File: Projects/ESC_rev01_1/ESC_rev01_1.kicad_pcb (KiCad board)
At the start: 2 copper layers, 65 x 56 mm, 4 parts

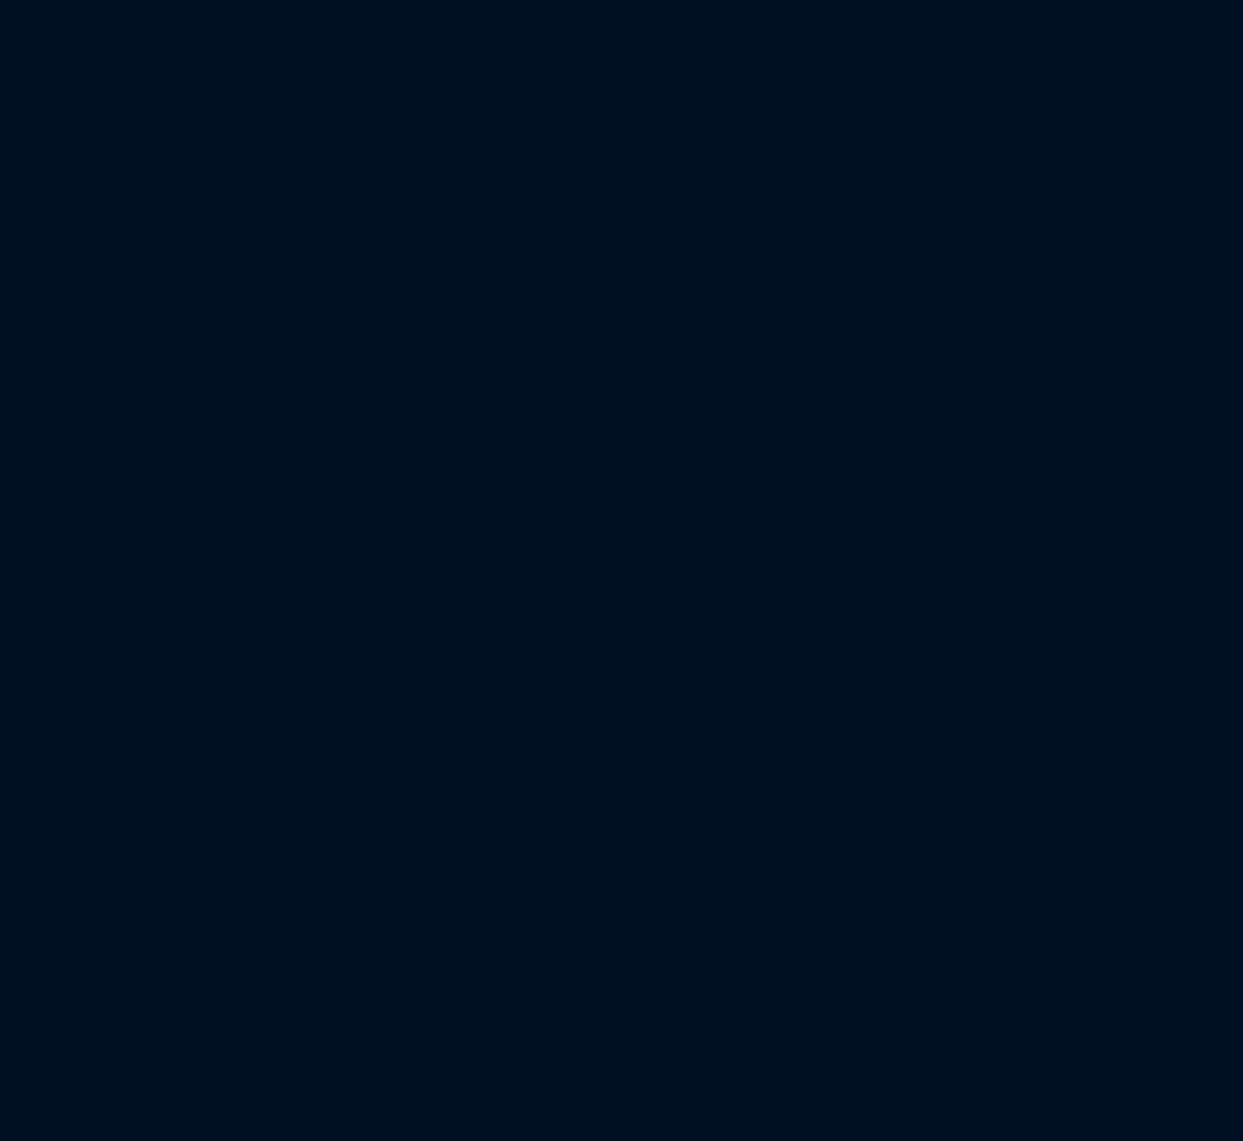
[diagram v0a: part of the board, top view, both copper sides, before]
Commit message: Update 07
Schematic is ready
INPUT PROTECTION schematic created
MOSFETs schematic created
CAN schematic created
FILTERs schematic created
MECHANICAL schematic created
STEP-DOWN schematic created
Footprints, 3D models are added and corrected (major issues)
Component placement started
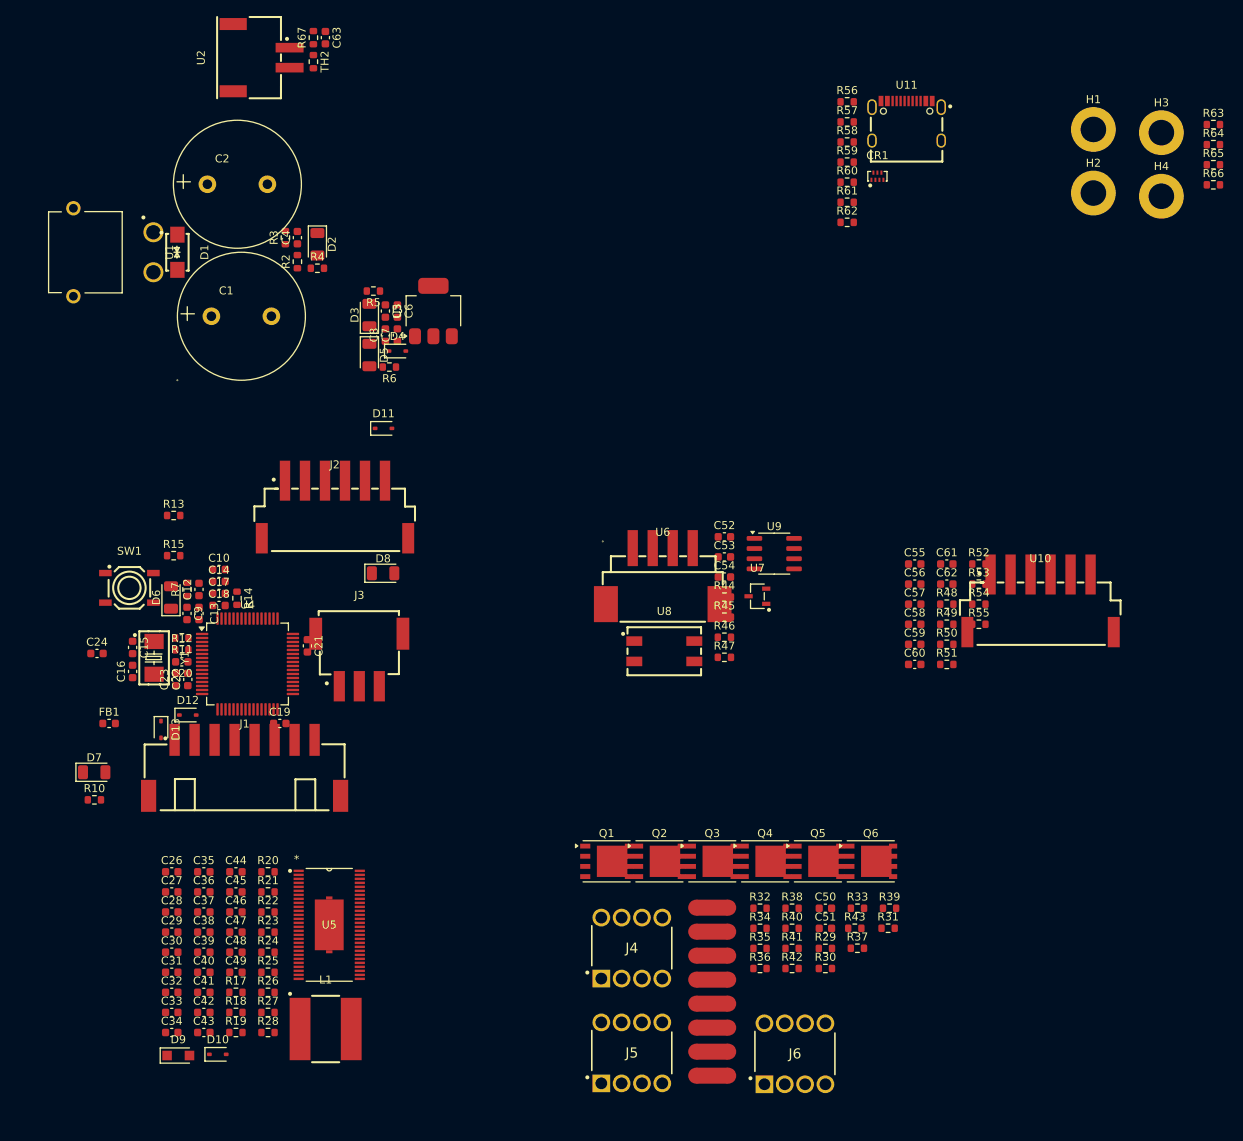
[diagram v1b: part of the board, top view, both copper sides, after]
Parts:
- added C1: LKMI2501K821MF, DF_ESC_rev01_1:CAP-TH_BD16.0-P7.50-D1.2-FD, F.Cu at (453.5, 69.0)
- added C10: 100n, Capacitor_SMD:C_0603_1608Metric, F.Cu at (450.7, 100.7)
- added C12: 100n, Capacitor_SMD:C_0603_1608Metric, F.Cu at (448.2, 103.2)
- added C13: 100n, Capacitor_SMD:C_0603_1608Metric, F.Cu at (448.2, 106.2)
- added C14: 100n, Capacitor_SMD:C_0603_1608Metric, F.Cu at (450.7, 102.2)
- added C15: C, Capacitor_SMD:C_0603_1608Metric, F.Cu at (439.9, 110.4)
- added C16: 10p, Capacitor_SMD:C_0603_1608Metric, F.Cu at (439.9, 113.4)
- added C17: 100n, Capacitor_SMD:C_0603_1608Metric, F.Cu at (450.7, 103.7)
- added C18: 100n, Capacitor_SMD:C_0603_1608Metric, F.Cu at (450.7, 105.2)
- added C19: 2u2, Capacitor_SMD:C_0603_1608Metric, F.Cu at (458.3, 119.9)
- added C2: LKMI2501K821MF, DF_ESC_rev01_1:CAP-TH_BD16.0-P7.50-D1.2-FD, F.Cu at (453.0, 52.5)
- added C20: 100n, Capacitor_SMD:C_0603_1608Metric, F.Cu at (446.1, 112.2)
- added C21: 2u2, Capacitor_SMD:C_0603_1608Metric, F.Cu at (461.8, 110.2)
- added C22: 100n, Capacitor_SMD:C_0603_1608Metric, F.Cu at (446.8, 114.4)
- added C23: 1u, Capacitor_SMD:C_0603_1608Metric, F.Cu at (445.3, 114.4)
- added C24: 100n, Capacitor_SMD:C_0603_1608Metric, F.Cu at (435.5, 111.2)
- added C26: 2u2, Capacitor_SMD:C_0603_1608Metric, F.Cu at (444.8, 138.4)
- added C27: 2u2, Capacitor_SMD:C_0603_1608Metric, F.Cu at (444.8, 141.0)
- added C28: 6n8, Capacitor_SMD:C_0603_1608Metric, F.Cu at (444.8, 143.5)
- added C29: 2u2, Capacitor_SMD:C_0603_1608Metric, F.Cu at (444.8, 146.0)
- added C30: 2u2, Capacitor_SMD:C_0603_1608Metric, F.Cu at (444.8, 148.5)
- added C31: 2u2, Capacitor_SMD:C_0603_1608Metric, F.Cu at (444.8, 151.0)
- added C32: 120p, Capacitor_SMD:C_0603_1608Metric, F.Cu at (444.8, 153.5)
- added C33: 2u2, Capacitor_SMD:C_0603_1608Metric, F.Cu at (444.8, 156.0)
- added C34: 10u, Capacitor_SMD:C_0603_1608Metric, F.Cu at (444.8, 158.5)
- added C35: 100n, Capacitor_SMD:C_0603_1608Metric, F.Cu at (448.8, 138.4)
- added C36: 10u, Capacitor_SMD:C_0603_1608Metric, F.Cu at (448.8, 141.0)
- added C37: 10u, Capacitor_SMD:C_0603_1608Metric, F.Cu at (448.8, 143.5)
- added C38: 10u, Capacitor_SMD:C_0603_1608Metric, F.Cu at (448.8, 146.0)
- added C39: 10u, Capacitor_SMD:C_0603_1608Metric, F.Cu at (448.8, 148.5)
- added C4: 100n, Capacitor_SMD:C_0603_1608Metric, F.Cu at (460.5, 59.2)
- added C40: 10u, Capacitor_SMD:C_0603_1608Metric, F.Cu at (448.8, 151.0)
- added C41: 10u, Capacitor_SMD:C_0603_1608Metric, F.Cu at (448.8, 153.5)
- added C42: 10u, Capacitor_SMD:C_0603_1608Metric, F.Cu at (448.8, 156.0)
- added C43: 10u, Capacitor_SMD:C_0603_1608Metric, F.Cu at (448.8, 158.5)
- added C44: 100n, Capacitor_SMD:C_0603_1608Metric, F.Cu at (452.8, 138.4)
- added C45: 10u, Capacitor_SMD:C_0603_1608Metric, F.Cu at (452.8, 141.0)
- added C46: 10u, Capacitor_SMD:C_0603_1608Metric, F.Cu at (452.8, 143.5)
- added C47: 100n, Capacitor_SMD:C_0603_1608Metric, F.Cu at (452.8, 146.0)
- added C48: 10u, Capacitor_SMD:C_0603_1608Metric, F.Cu at (452.8, 148.5)
- added C49: 100n, Capacitor_SMD:C_0603_1608Metric, F.Cu at (452.8, 151.0)
- added C5: 1u, Capacitor_SMD:C_0603_1608Metric, F.Cu at (471.5, 68.3)
- added C50: 2u2, Capacitor_SMD:C_0603_1608Metric, F.Cu at (526.5, 143.0)
- added C51: 2n2, Capacitor_SMD:C_0603_1608Metric, F.Cu at (526.5, 145.5)
- added C52: 60p, Capacitor_SMD:C_0603_1608Metric, F.Cu at (513.9, 96.6)
- added C53: 60p, Capacitor_SMD:C_0603_1608Metric, F.Cu at (513.9, 99.1)
- added C54: 2u2, Capacitor_SMD:C_0603_1608Metric, F.Cu at (513.9, 101.6)
- added C55: 4n7, Capacitor_SMD:C_0603_1608Metric, F.Cu at (537.7, 100.0)
- added C56: 4n7, Capacitor_SMD:C_0603_1608Metric, F.Cu at (537.7, 102.5)
- added C57: 4n7, Capacitor_SMD:C_0603_1608Metric, F.Cu at (537.7, 105.0)
- added C58: 4n7, Capacitor_SMD:C_0603_1608Metric, F.Cu at (537.7, 107.5)
- added C59: 100n, Capacitor_SMD:C_0603_1608Metric, F.Cu at (537.7, 110.0)
- added C6: 1u, Capacitor_SMD:C_0603_1608Metric, F.Cu at (473.0, 68.3)
- added C60: 100n, Capacitor_SMD:C_0603_1608Metric, F.Cu at (537.7, 112.5)
- added C61: 100n, Capacitor_SMD:C_0603_1608Metric, F.Cu at (541.7, 100.0)
- added C62: 100n, Capacitor_SMD:C_0603_1608Metric, F.Cu at (541.7, 102.5)
- added C63: 100n, Capacitor_SMD:C_0603_1608Metric, F.Cu at (464.0, 34.2)
- added C7: 1u, Capacitor_SMD:C_0603_1608Metric, F.Cu at (473.0, 71.3)
- added C8: 1u, Capacitor_SMD:C_0603_1608Metric, F.Cu at (471.5, 71.3)
- added C9: C, Capacitor_SMD:C_0603_1608Metric, F.Cu at (446.7, 106.2)
- added CR1: PUSB3AB6Z, DF_ESC_rev01_1:XSON-7_L2.2-W1.2-P0.50-BL, F.Cu at (533.0, 51.5)
- added D1: SMA6J60CA-Q, DF_ESC_rev01_1:SMA_L4.4-W2.8-LS5.1-BI, F.Cu at (445.5, 61.0)
- added D10: BAT60A, Diode_SMD:D_SOD-323, F.Cu at (450.6, 161.3)
- added D11: BAT60A, Diode_SMD:D_SOD-323, F.Cu at (471.3, 83.0)
- added D12: BAT60A, Diode_SMD:D_SOD-323, F.Cu at (446.8, 118.8)
- added D13: BAT60A, Diode_SMD:D_SOD-323, F.Cu at (443.4, 120.7)
- added D2: LED_G, LED_SMD:LED_1206_3216Metric, F.Cu at (463.0, 60.0)
- added D3: LED_G, LED_SMD:LED_1206_3216Metric, F.Cu at (469.5, 68.8)
- added D4: BAT60A, Diode_SMD:D_SOD-323, F.Cu at (473.0, 73.3)
- added D5: LED_G, LED_SMD:LED_1206_3216Metric, F.Cu at (469.5, 73.8)
- added D6: LED_G, LED_SMD:LED_1206_3216Metric, F.Cu at (444.7, 104.2)
- added D7: LED_G, LED_SMD:LED_1206_3216Metric, F.Cu at (435.1, 126.0)
- added D8: LED_R, LED_SMD:LED_1206_3216Metric, F.Cu at (471.2, 101.1)
- added D9: PMEG6020ER, Diode_SMD:Nexperia_CFP3_SOD-123W, F.Cu at (445.6, 161.4)
- added FB1: FerriteBead, Inductor_SMD:L_0603_1608Metric, F.Cu at (437.0, 119.9)
- added H1: MountingHole_Pad, MountingHole:MountingHole_3.2mm_M3_DIN965_Pad, F.Cu at (560.0, 45.6)
- added H2: MountingHole_Pad, MountingHole:MountingHole_3.2mm_M3_DIN965_Pad, F.Cu at (560.0, 53.6)
- added H3: MountingHole_Pad, MountingHole:MountingHole_3.2mm_M3_DIN965_Pad, F.Cu at (568.5, 46.0)
- added H4: MountingHole_Pad, MountingHole:MountingHole_3.2mm_M3_DIN965_Pad, F.Cu at (568.5, 54.0)
- added J1: XH-2PWBPZ, DF_ESC_rev01_1:CONN-SMD_8P-P2.50_HX25003-8AWB, F.Cu at (453.9, 125.5)
- added J2: Conn_01x06, DF_ESC_rev01_1:CONN-SMD_6P-P2.50_DEALON_XH-6PWB, F.Cu at (465.2, 93.2)
- added J3: Conn_01x03, DF_ESC_rev01_1:CONN-SMD_XH-3AWB, F.Cu at (468.2, 112.0)
- added J4: Conn_01x01, DF_ESC_rev01_1:WE_7461084, F.Cu at (498.5, 151.8)
- added J5: Conn_01x01, DF_ESC_rev01_1:WE_7461084, F.Cu at (498.5, 164.9)
- added J6: Conn_01x01, DF_ESC_rev01_1:WE_7461084, F.Cu at (518.9, 165.0)
- added L1: 22u, DF_ESC_rev01_1:IND-SMD_L7.8-W7.8_SDR0805, F.Cu at (464.0, 158.1)
- added NT1: NetTie_2, NetTie:NetTie-2_SMD_Pad2.0mm, F.Cu at (512.4, 142.9)
- added NT2: NetTie_2, NetTie:NetTie-2_SMD_Pad2.0mm, F.Cu at (512.4, 145.9)
- added NT3: NetTie_2, NetTie:NetTie-2_SMD_Pad2.0mm, F.Cu at (512.4, 148.9)
- added NT4: NetTie_2, NetTie:NetTie-2_SMD_Pad2.0mm, F.Cu at (512.4, 151.9)
- added NT5: NetTie_2, NetTie:NetTie-2_SMD_Pad2.0mm, F.Cu at (512.4, 154.9)
- added NT6: NetTie_2, NetTie:NetTie-2_SMD_Pad2.0mm, F.Cu at (512.4, 157.9)
- added NT7: NetTie_2, NetTie:NetTie-2_SMD_Pad2.0mm, F.Cu at (512.4, 160.9)
- added NT8: NetTie_2, NetTie:NetTie-2_SMD_Pad2.0mm, F.Cu at (512.4, 163.9)
- added Q1: HSBA15810C, Package_SO:PowerPAK_SO-8_Single, F.Cu at (499.2, 137.1)
- added Q2: HSBA15810C, Package_SO:PowerPAK_SO-8_Single, F.Cu at (505.8, 137.1)
- added Q3: HSBA15810C, Package_SO:PowerPAK_SO-8_Single, F.Cu at (512.4, 137.1)
- added Q4: HSBA15810C, Package_SO:PowerPAK_SO-8_Single, F.Cu at (519.0, 137.1)
- added Q5: HSBA15810C, Package_SO:PowerPAK_SO-8_Single, F.Cu at (525.6, 137.1)
- added Q6: HSBA15810C, Package_SO:PowerPAK_SO-8_Single, F.Cu at (532.2, 137.1)
- added R10: 1k, Resistor_SMD:R_0603_1608Metric, F.Cu at (435.1, 129.4)
- added R11: R, Resistor_SMD:R_0603_1608Metric, F.Cu at (446.1, 109.2)
- added R12: 0R, Resistor_SMD:R_0603_1608Metric, F.Cu at (446.1, 110.7)
- added R13: 1k, Resistor_SMD:R_0603_1608Metric, F.Cu at (445.0, 93.9)
- added R14: 0R, Resistor_SMD:R_0603_1608Metric, F.Cu at (453.0, 104.2)
- added R15: 2k2, Resistor_SMD:R_0603_1608Metric, F.Cu at (445.0, 98.9)
- added R17: 16k2, Resistor_SMD:R_0603_1608Metric, F.Cu at (452.8, 153.5)
- added R18: 10k, Resistor_SMD:R_0603_1608Metric, F.Cu at (452.8, 156.0)
- added R19: 205k, Resistor_SMD:R_0603_1608Metric, F.Cu at (452.8, 158.5)
- added R2: 39k, Resistor_SMD:R_0603_1608Metric, F.Cu at (460.5, 62.2)
- added R20: 1M, Resistor_SMD:R_0603_1608Metric, F.Cu at (456.8, 138.4)
- added R21: 18k, Resistor_SMD:R_0603_1608Metric, F.Cu at (456.8, 141.0)
- added R22: 3k3, Resistor_SMD:R_0603_1608Metric, F.Cu at (456.8, 143.5)
- added R23: 18k, Resistor_SMD:R_0603_1608Metric, F.Cu at (456.8, 146.0)
- added R24: 3k3, Resistor_SMD:R_0603_1608Metric, F.Cu at (456.8, 148.5)
- added R25: 18k, Resistor_SMD:R_0603_1608Metric, F.Cu at (456.8, 151.0)
- added R26: 3k3, Resistor_SMD:R_0603_1608Metric, F.Cu at (456.8, 153.5)
- added R27: 18k, Resistor_SMD:R_0603_1608Metric, F.Cu at (456.8, 156.0)
- added R28: 3k3, Resistor_SMD:R_0603_1608Metric, F.Cu at (456.8, 158.5)
- added R29: 4R7, Resistor_SMD:R_0603_1608Metric, F.Cu at (526.5, 148.0)
- added R3: 2k2, Resistor_SMD:R_0603_1608Metric, F.Cu at (459.0, 59.2)
- added R30: 4R7, Resistor_SMD:R_0603_1608Metric, F.Cu at (526.5, 150.5)
- added R31: 100R, Resistor_SMD:R_0603_1608Metric, F.Cu at (534.3, 145.5)
- added R32: 100R, Resistor_SMD:R_0603_1608Metric, F.Cu at (518.3, 143.0)
- added R33: 39k, Resistor_SMD:R_0603_1608Metric, F.Cu at (530.5, 143.0)
- added R34: 0R001, Resistor_SMD:R_0603_1608Metric, F.Cu at (518.3, 145.5)
- added R35: 4R7, Resistor_SMD:R_0603_1608Metric, F.Cu at (518.3, 148.0)
- added R36: 4R7, Resistor_SMD:R_0603_1608Metric, F.Cu at (518.3, 150.5)
- added R37: 100R, Resistor_SMD:R_0603_1608Metric, F.Cu at (530.5, 148.0)
- added R38: 100R, Resistor_SMD:R_0603_1608Metric, F.Cu at (522.3, 143.0)
- added R39: 39k, Resistor_SMD:R_0603_1608Metric, F.Cu at (534.5, 143.0)
- added R4: 39k, Resistor_SMD:R_0603_1608Metric, F.Cu at (463.0, 63.0)
- added R40: 0R001, Resistor_SMD:R_0603_1608Metric, F.Cu at (522.3, 145.5)
- added R41: 4R7, Resistor_SMD:R_0603_1608Metric, F.Cu at (522.3, 148.0)
- added R42: 4R7, Resistor_SMD:R_0603_1608Metric, F.Cu at (522.3, 150.5)
- added R43: 39k, Resistor_SMD:R_0603_1608Metric, F.Cu at (530.2, 145.5)
- added R44: 120R, Resistor_SMD:R_0603_1608Metric, F.Cu at (513.9, 104.1)
- added R45: 10R, Resistor_SMD:R_0603_1608Metric, F.Cu at (513.9, 106.6)
- added R46: 10R, Resistor_SMD:R_0603_1608Metric, F.Cu at (513.9, 109.1)
- added R47: 10k, Resistor_SMD:R_0603_1608Metric, F.Cu at (513.9, 111.6)
- added R48: 2k2, Resistor_SMD:R_0603_1608Metric, F.Cu at (541.7, 105.0)
- added R49: 2k2, Resistor_SMD:R_0603_1608Metric, F.Cu at (541.7, 107.5)
- added R5: 1k, Resistor_SMD:R_0603_1608Metric, F.Cu at (470.0, 65.8)
- added R50: 2k2, Resistor_SMD:R_0603_1608Metric, F.Cu at (541.7, 110.0)
- added R51: 10k, Resistor_SMD:R_0603_1608Metric, F.Cu at (541.7, 112.5)
- added R52: 10k, Resistor_SMD:R_0603_1608Metric, F.Cu at (545.7, 100.0)
- added R53: 10k, Resistor_SMD:R_0603_1608Metric, F.Cu at (545.7, 102.5)
- added R54: 10k, Resistor_SMD:R_0603_1608Metric, F.Cu at (545.7, 105.0)
- added R55: 0R, Resistor_SMD:R_0603_1608Metric, F.Cu at (545.7, 107.5)
- added R56: 0R, Resistor_SMD:R_0603_1608Metric, F.Cu at (529.2, 42.2)
- added R57: 0R, Resistor_SMD:R_0603_1608Metric, F.Cu at (529.2, 44.7)
- added R58: 0R, Resistor_SMD:R_0603_1608Metric, F.Cu at (529.2, 47.2)
- added R59: 5k1, Resistor_SMD:R_0603_1608Metric, F.Cu at (529.2, 49.7)
- added R6: 1k, Resistor_SMD:R_0603_1608Metric, F.Cu at (472.0, 75.3)
- added R60: 5k1, Resistor_SMD:R_0603_1608Metric, F.Cu at (529.2, 52.2)
- added R61: 22R, Resistor_SMD:R_0603_1608Metric, F.Cu at (529.2, 54.7)
- added R62: 22R, Resistor_SMD:R_0603_1608Metric, F.Cu at (529.2, 57.3)
- added R63: 0R, Resistor_SMD:R_0603_1608Metric, F.Cu at (575.0, 45.0)
- added R64: 0R, Resistor_SMD:R_0603_1608Metric, F.Cu at (575.0, 47.5)
- added R65: 0R, Resistor_SMD:R_0603_1608Metric, F.Cu at (575.0, 50.1)
- added R66: 0R, Resistor_SMD:R_0603_1608Metric, F.Cu at (575.0, 52.6)
- added R67: 2k2, Resistor_SMD:R_0603_1608Metric, F.Cu at (462.5, 34.2)
- added R7: 1k, Resistor_SMD:R_0603_1608Metric, F.Cu at (446.7, 103.2)
- added SW1: PTS526SK15SMTR2LFS, DF_ESC_rev01_1:SW-SMD_4P-L5.2-W5.2-P3.70-LS6.4, F.Cu at (439.5, 103.0)
- added TH2: 10k, Resistor_SMD:R_0603_1608Metric, F.Cu at (462.5, 37.2)
- added U1: XT30PW-M, DF_ESC_rev01_1:CONN-TH_XT30PW-M, F.Cu at (437.5, 61.0)
- added U10: Conn_01x04_2mnt, DF_ESC_rev01_1:CONN-SMD_6P-P2.50_DEALON_XH-6PWB, F.Cu at (553.4, 104.9)
- added U11: TYPE-C-31-M-12, DF_ESC_rev01_1:USB-C_SMD-TYPE-C-31-M-12_1, F.Cu at (536.7, 44.6)
- added U2: XH-2PWBPZ, DF_ESC_rev01_1:CONN-SMD_XH-2PWBPZ, F.Cu at (456.0, 36.7)
- added U3: AMS1117-3.3, Package_TO_SOT_SMD:SOT-223-3_TabPin2, F.Cu at (477.5, 68.3)
- added U4: STM32F405RGTx, Package_QFP:LQFP-64_10x10mm_P0.5mm, F.Cu at (454.3, 112.5)
- added U5: DRV8302DCA, DF_ESC_rev01_1:DCA56_6P35X3P61, F.Cu at (464.5, 145.1)
- added U6: Conn_01x04_2mnt, DF_ESC_rev01_1:CONN-SMD_S4B-XH-SM4-TB-LF-SN, F.Cu at (506.2, 101.5)
- added U7: ESDCAN24-2BLY, DF_ESC_rev01_1:SOT-23-3_L3.0-W1.7-P0.95-LS2.9-BR, F.Cu at (518.0, 104.0)
- added U8: 744227S, DF_ESC_rev01_1:FILTER-SMD_4P-L9.2-W6.0-P2.54-TL, F.Cu at (506.4, 110.9)
- added U9: SN65HVD230, Package_SO:SOIC-8_3.9x4.9mm_P1.27mm, F.Cu at (520.1, 98.7)
- added Y1: 8M 10ppm, DF_ESC_rev01_1:CRYSTAL-SMD_L5.0-W3.2, F.Cu at (442.6, 111.7)
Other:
- board text added: "CAN"
- board text added: "FILTERS"
- board text added: "INPUT PROTECTION"
- board text added: "MCU"
- board text added: "MOSFET DRIVER"
- board text added: "MOSFETs"
- board text added: "MOUNTING HOLES"
- board text added: "NTC THERMISTOR"
- board text added: "STEP-DOWN"
- board text added: "USB"

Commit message: Update 08
Component placement is almost done
Check one more time and correct if needed
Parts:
- removed MH1, MH2, MH3, MH4: MountingHole_2.7mm_M2.5, MountingHole:MountingHole_2.7mm_M2.5
- C1, C2: moved to B.Cu
- moved R63 411.1 mm to (185.0, 175.0)
- moved H1 401.4 mm to (180.0, 175.0)
- moved R64 395.0 mm to (185.0, 110.0)
- moved H2 384.2 mm to (180.0, 110.0)
- moved U10 345.6 mm to (214.7, 174.1)
- moved R54 340.7 mm to (210.1, 163.6), turned to 180 degrees
- moved R53 338.2 mm to (213.1, 163.6), turned to 180 degrees
- moved C61 337.1 mm to (210.0, 160.4)
- moved R50 335.7 mm to (210.0, 161.9)
- moved R52 335.6 mm to (216.1, 163.4), turned to 180 degrees
- moved R66 333.3 mm to (265.0, 175.0), turned to 180 degrees
- moved C57 333.1 mm to (210.0, 165.1), turned to 180 degrees
- moved R49 333.1 mm to (213.1, 162.0)
- moved R55 331.5 mm to (219.2, 165.2)
- moved C56 330.6 mm to (213.1, 165.1), turned to 180 degrees
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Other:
- board size 65 x 56 mm -> 100 x 75 mm
- copper layers 2 -> 4
- board text removed: "Extend PCB edge 0.5mm if using SMT header"
- board text removed: "FILTERS"
- board text removed: "INPUT PROTECTION"
- board text removed: "MCU"
- board text removed: "MOSFET DRIVER"
- board text removed: "MOSFETs"
- board text removed: "MOUNTING HOLES"
- board text removed: "NTC THERMISTOR"
- board text removed: "STEP-DOWN"
- board text removed: "USB"

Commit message: Update 09
Components placement finished
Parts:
- removed the R7 at (205.1, 136.8)
- added D9: SD05C-7, Diode_SMD:D_SOD-323_HandSoldering, F.Cu at (188.2, 138.5)
- added R11: 2k2, Resistor_SMD:R_0603_1608Metric, F.Cu at (193.0, 134.4)
- C14: renamed from C15; value C -> 10p
- C42: renamed from C44; moved to B.Cu
- C45: renamed from C47; moved to B.Cu
- C47: renamed from C49; moved to B.Cu
- C48: renamed from C50; moved to B.Cu
- C49: renamed from C51; moved to B.Cu
- C9: value C -> 10u
- D6: value LED_G -> PESD3V3X1BL; footprint LED_SMD:LED_1206_3216Metric -> DF_ESC_rev01_1:D_SOD-882_BI
- NT1, NT4, NT7: footprint NetTie:NetTie-2_SMD_Pad2.0mm -> NetTie:NetTie-2_SMD_Pad0.5mm
- NT2, NT3, NT5, NT6, NT8: footprint NetTie:NetTie-2_SMD_Pad2.0mm -> DF_ESC_rev01_1:NetTie-2_SMD_Pad_4.0x2.0mm
- Q1, Q2, Q3, Q4, Q5, Q6: footprint Package_SO:PowerPAK_SO-8_Single -> DF_ESC_rev01_1:PQFN-8_L6.0-W5.0-P1.27-LS6.0-BL
- R12: renamed from R14; value 0R -> 100R
- R28: renamed from R31; moved to B.Cu
- R29: renamed from R32; moved to B.Cu
- R31: renamed from R34; footprint Resistor_SMD:R_0603_1608Metric -> DF_ESC_rev01_1:RES_VISHAY_WSLP27261L000
- R34: renamed from R37; moved to B.Cu
- R35: renamed from R38; moved to B.Cu
- R37: renamed from R40; footprint Resistor_SMD:R_0603_1608Metric -> DF_ESC_rev01_1:RES_VISHAY_WSLP27261L000
- R8: renamed from R11; value R -> 0R
- Y1: value 8M 10ppm -> 8M 10ppm X50328MSB2GI
- moved R58 33.0 mm to (215.4, 138.8)
- moved R59 33.0 mm to (213.9, 138.8)
- moved R20 32.4 mm to (264.0, 134.5), turned to 180 degrees
- moved R21 30.1 mm to (264.0, 136.2), turned to 180 degrees
- moved D8 29.1 mm to (225.5, 177.0), turned to 90 degrees
- moved R19 28.5 mm to (222.8, 144.8), turned to 90 degrees
- moved D14 26.5 mm to (227.0, 141.0), turned to 0 degrees
- moved R18 25.9 mm to (224.5, 144.8)
- moved R24 25.9 mm to (264.0, 169.5), turned to 180 degrees
- moved R25 25.9 mm to (264.0, 171.2), turned to 180 degrees
- moved D11 24.2 mm to (228.8, 177.0), turned to 90 degrees
- moved R10 24.1 mm to (228.8, 173.0), turned to -90 degrees
- moved R7 24.0 mm to (225.5, 173.0), turned to -90 degrees
- moved C44 23.2 mm to (226.2, 143.7), turned to 90 degrees
- moved R34 22.9 mm to (249.7, 157.0)
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- renumbered C12 to C11, C13 to C12, C14 to C13, C16 to C15, C17 to C16, C18 to C17, C19 to C18, C20 to C19, C21 to C20, C22 to C21, C23 to C22, C24 to C23, C26 to C24, C27 to C25, C28 to C26, C29 to C27, C30 to C28, C31 to C29, C63 to C3, C32 to C30, C33 to C31, C34 to C32, C35 to C33, C36 to C34, C37 to C35, C38 to C36, C39 to C37, C40 to C38, C41 to C39, C42 to C40, C43 to C41, C45 to C43, C46 to C44, C48 to C46, C52 to C50, C53 to C51, C54 to C52, C55 to C53, C56 to C54, C57 to C55, C58 to C56, C59 to C57, C60 to C58, C61 to C59, C62 to C60, D13 to D10, D8 to D11, D11 to D12, D9 to D13, D10 to D14, D12 to D7, D7 to D8, U1 to J1, U10 to J10, U11 to J11, U2 to J2, J1 to J3, J2 to J4, J3 to J5, J4 to J6, J5 to J7, J6 to J8, U6 to J9, R67 to R1, R13 to R10, R15 to R13, R17 to R14, R18 to R15, R19 to R16, R20 to R17, R21 to R18, R22 to R19, R23 to R20, R24 to R21, R25 to R22, R26 to R23, R27 to R24, R28 to R25, R29 to R26, R30 to R27, R33 to R30, R35 to R32, R36 to R33, R39 to R36, R41 to R38, R42 to R39, R43 to R40, R44 to R41, R45 to R42, R46 to R43, R47 to R44, R48 to R45, R49 to R46, R50 to R47, R51 to R48, R52 to R49, R53 to R50, R54 to R51, R55 to R52, R56 to R53, R57 to R54, R58 to R55, R59 to R56, R60 to R57, R61 to R58, R62 to R59, R63 to R60, R64 to R61, R65 to R62, R66 to R63, R10 to R7, R12 to R9, TH2 to TH1, U3 to U1, U4 to U2, U5 to U3, U7 to U4, U8 to U5, U9 to U6
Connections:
- net Net-(C15-Pad1) renamed /[04] - MCU/PH_0
- net Net-(C16-Pad1) renamed /[04] - MCU/PH_1
- net Net-(U4-BOOT0) renamed /[04] - MCU/BOOT
- net Net-(U4-VCAP_1) renamed /[04] - MCU/VCAP_1
- net Net-(U4-VCAP_2) renamed /[04] - MCU/VCAP_2
- net Net-(U4-VDDA) renamed /[04] - MCU/+3V3_A
- D6 pad 2: Net-(D6-A) -> /[04] - MCU/+3V3_COM
- J3 pad 5: /[04] - MCU/TX_SDA_NSS -> /[04] - MCU/RX_SCL_MOSI
- J3 pad 6: /[04] - MCU/RX_SCL_MOSI -> /[04] - MCU/TX_SDA_NSS
- R12 pad 1: +3V3 -> GND
- R31 pad 1: /[06] - MOSFETs/SH1_N -> /[06] - MOSFETs/SH1_P
- R31 pad 2: /[06] - MOSFETs/SH1_P -> /[06] - MOSFETs/SH1_N
- R37 pad 1: /[06] - MOSFETs/SH2_N -> /[06] - MOSFETs/SH2_P
- R37 pad 2: /[06] - MOSFETs/SH2_P -> /[06] - MOSFETs/SH2_N
- SW1 pad 1: GND -> Net-(R11-Pad1)
- SW1 pad 2: GND -> Net-(R11-Pad1)
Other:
- board text added: "COM"
- board text added: "FILTERS"
- board text added: "SENSORS"

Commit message: Update 10
-Rules added (for signal, differential pair USB and CAN, power traces)
-Stackup corrected
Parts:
- moved R28 21.7 mm to (241.0, 160.2), turned to 0 degrees
- moved C48 20.0 mm to (236.6, 159.1), turned to 90 degrees
- moved R29 18.5 mm to (241.0, 158.0), turned to 0 degrees
- moved C49 12.1 mm to (236.6, 163.1), turned to 90 degrees
- moved R34 11.1 mm to (241.0, 164.0), turned to 0 degrees
- moved R35 7.54 mm to (241.0, 162.0), turned to 0 degrees
- moved C24 2.11 mm to (221.4, 155.0)
- moved C25 2.11 mm to (221.4, 159.6)
- moved C27 2.11 mm to (221.4, 156.6)
- moved C28 2.11 mm to (221.4, 158.1)
- moved C29 2.11 mm to (221.4, 163.1)
- moved C30 2.11 mm to (221.4, 150.5)
- moved C31 2.11 mm to (221.4, 161.1)
- moved C32 2.11 mm to (229.6, 166.3)
- moved C33 2.11 mm to (234.9, 151.3)
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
